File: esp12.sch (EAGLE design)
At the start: 26 parts, among them IC1 117\33

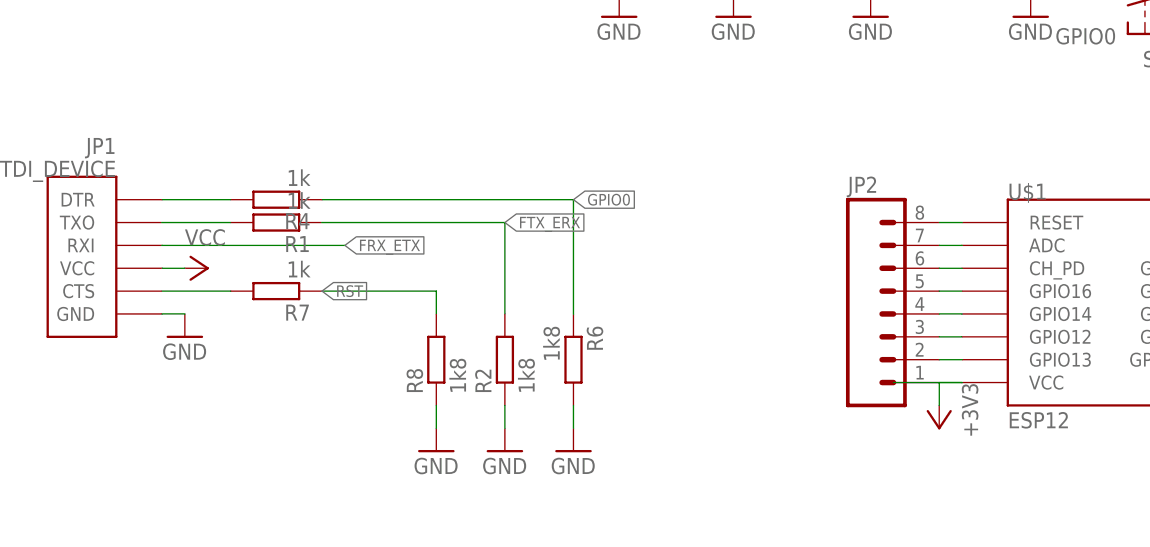
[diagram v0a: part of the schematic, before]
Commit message: gitignore and ADC 5V to 1.8V conversion
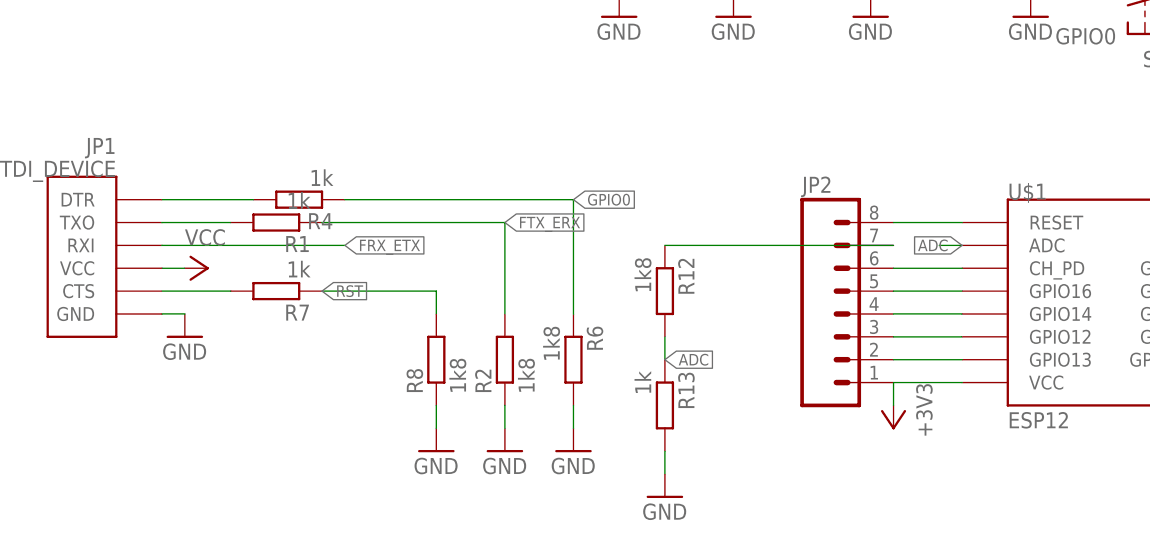
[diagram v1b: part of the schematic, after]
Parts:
- added R12: 1k8, resistor:R-EU_M1206
- added R13: 1k, resistor:R-EU_M1206
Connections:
- new net ADC: R12.2, R13.1, U$1.ADC
- net GND: now also R13.2
- net N$9: now also R12.1; no longer U$1.ADC
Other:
- moved on the sheet: JP2, R4
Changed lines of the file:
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@@
 <part name="GND11" library="supply1" deviceset="GND" device=""/>
 <part name="R11" library="resistor" deviceset="R-EU_" device="M1206" value="10k"/>
+<part name="R12" library="resistor" deviceset="R-EU_" device="M1206" value="1k8"/>
+<part name="R13" library="resistor" deviceset="R-EU_" device="M1206" value="1k"/>
+<part name="GND14" library="supply1" deviceset="GND" device=""/>
 </parts>
 <sheets>
@@
 <instance part="GND7" gate="1" x="63.5" y="71.12"/>
 <instance part="U$1" gate="G$1" x="73.66" y="40.64"/>
-<instance part="+3V2" gate="G$1" x="53.34" y="25.4" rot="R180"/>
-<instance part="JP2" gate="G$1" x="48.26" y="38.1"/>
+<instance part="+3V2" gate="G$1" x="48.26" y="25.4" rot="R180"/>
+<instance part="JP2" gate="G$1" x="43.18" y="38.1"/>
 <instance part="JP3" gate="G$1" x="96.52" y="38.1" rot="MR0"/>
 <instance part="S2" gate="1" x="76.2" y="88.9" rot="R90"/>
@@
 <instance part="GND10" gate="1" x="63.5" y="104.14"/>
 <instance part="+3V6" gate="G$1" x="96.52" y="116.84"/>
-<instance part="R4" gate="G$1" x="-20.32" y="50.8" rot="R180"/>
+<instance part="R4" gate="G$1" x="-17.78" y="50.8" rot="R180"/>
 <instance part="R6" gate="G$1" x="12.7" y="33.02" rot="R270"/>
 <instance part="GND12" gate="1" x="12.7" y="22.86"/>
@@
 <instance part="GND11" gate="1" x="-12.7" y="104.14" rot="R180"/>
 <instance part="R11" gate="G$1" x="-12.7" y="91.44" rot="R270"/>
+<instance part="R12" gate="G$1" x="22.86" y="40.64" rot="R270"/>
+<instance part="R13" gate="G$1" x="22.86" y="27.94" rot="R270"/>
+<instance part="GND14" gate="1" x="22.86" y="17.78"/>
 </instances>
 <busses>
@@
 <wire x1="-12.7" y1="101.6" x2="-12.7" y2="96.52" width="0.1524" layer="91"/>
 </segment>
+<segment>
+<pinref part="R13" gate="G$1" pin="2"/>
+<pinref part="GND14" gate="1" pin="GND"/>
+<wire x1="22.86" y1="22.86" x2="22.86" y2="20.32" width="0.1524" layer="91"/>
+</segment>
 </net>
 <net name="+3V3" class="0">
@@
 <pinref part="JP2" gate="G$1" pin="1"/>
 <pinref part="JP2" gate="G$1" pin="1"/>
-<wire x1="53.34" y1="30.48" x2="53.34" y2="27.94" width="0.1524" layer="91"/>
-<wire x1="48.26" y1="30.48" x2="55.88" y2="30.48" width="0.1524" layer="91"/>
-<wire x1="55.88" y1="30.48" x2="53.34" y2="30.48" width="0.1524" layer="91"/>
+<wire x1="48.26" y1="30.48" x2="48.26" y2="27.94" width="0.1524" layer="91"/>
+<wire x1="55.88" y1="30.48" x2="48.26" y2="30.48" width="0.1524" layer="91"/>
 </segment>
 <segment>
@@
 <pinref part="U$1" gate="G$1" pin="GPIO13"/>
 <pinref part="JP2" gate="G$1" pin="2"/>
-<wire x1="53.34" y1="33.02" x2="55.88" y2="33.02" width="0.1524" layer="91"/>
+<wire x1="48.26" y1="33.02" x2="55.88" y2="33.02" width="0.1524" layer="91"/>
 </segment>
 </net>
@@
 <pinref part="U$1" gate="G$1" pin="GPIO12"/>
 <pinref part="JP2" gate="G$1" pin="3"/>
-<wire x1="53.34" y1="35.56" x2="55.88" y2="35.56" width="0.1524" layer="91"/>
+<wire x1="48.26" y1="35.56" x2="55.88" y2="35.56" width="0.1524" layer="91"/>
 </segment>
 </net>
@@
 <pinref part="U$1" gate="G$1" pin="GPIO14"/>
 <pinref part="JP2" gate="G$1" pin="4"/>
-<wire x1="53.34" y1="38.1" x2="55.88" y2="38.1" width="0.1524" layer="91"/>
+<wire x1="48.26" y1="38.1" x2="55.88" y2="38.1" width="0.1524" layer="91"/>
 </segment>
 </net>
@@
 <pinref part="U$1" gate="G$1" pin="GPIO16"/>
 <pinref part="JP2" gate="G$1" pin="5"/>
-<wire x1="53.34" y1="40.64" x2="55.88" y2="40.64" width="0.1524" layer="91"/>
-</segment>
-</net>
-<net name="N$9" class="0">
-<segment>
-<pinref part="U$1" gate="G$1" pin="ADC"/>
-<pinref part="JP2" gate="G$1" pin="7"/>
-<wire x1="53.34" y1="45.72" x2="55.88" y2="45.72" width="0.1524" layer="91"/>
+<wire x1="48.26" y1="40.64" x2="55.88" y2="40.64" width="0.1524" layer="91"/>
 </segment>
 </net>
@@
 <pinref part="R6" gate="G$1" pin="1"/>
 <wire x1="12.7" y1="38.1" x2="12.7" y2="50.8" width="0.1524" layer="91"/>
-<wire x1="12.7" y1="50.8" x2="-15.24" y2="50.8" width="0.1524" layer="91"/>
+<wire x1="12.7" y1="50.8" x2="-12.7" y2="50.8" width="0.1524" layer="91"/>
 <label x="12.7" y="50.8" size="1.27" layer="95" xref="yes"/>
 </segment>
@@
 <pinref part="U$1" gate="G$1" pin="RESET"/>
 <pinref part="JP2" gate="G$1" pin="8"/>
-<wire x1="53.34" y1="48.26" x2="55.88" y2="48.26" width="0.1524" layer="91"/>
+<wire x1="48.26" y1="48.26" x2="55.88" y2="48.26" width="0.1524" layer="91"/>
 </segment>
 <segment>
@@
 <pinref part="JP1" gate="G$1" pin="DTR"/>
 <pinref part="R4" gate="G$1" pin="2"/>
-<wire x1="-25.4" y1="50.8" x2="-33.02" y2="50.8" width="0.1524" layer="91"/>
+<wire x1="-22.86" y1="50.8" x2="-33.02" y2="50.8" width="0.1524" layer="91"/>
 </segment>
 </net>
@@
 <pinref part="U$1" gate="G$1" pin="CH_PD"/>
 <pinref part="JP2" gate="G$1" pin="6"/>
-<wire x1="53.34" y1="43.18" x2="55.88" y2="43.18" width="0.1524" layer="91"/>
+<wire x1="48.26" y1="43.18" x2="55.88" y2="43.18" width="0.1524" layer="91"/>
 </segment>
 <segment>
@@
 </segment>
 </net>
+<net name="N$9" class="0">
+<segment>
+<pinref part="JP2" gate="G$1" pin="7"/>
+<pinref part="R12" gate="G$1" pin="1"/>
+<wire x1="22.86" y1="45.72" x2="48.26" y2="45.72" width="0.1524" layer="91"/>
+</segment>
+</net>
+<net name="ADC" class="0">
+<segment>
+<pinref part="U$1" gate="G$1" pin="ADC"/>
+<wire x1="55.88" y1="45.72" x2="53.34" y2="45.72" width="0.1524" layer="91"/>
+<label x="55.88" y="45.72" size="1.27" layer="95" rot="R180" xref="yes"/>
+</segment>
+<segment>
+<pinref part="R12" gate="G$1" pin="2"/>
+<pinref part="R13" gate="G$1" pin="1"/>
+<wire x1="22.86" y1="35.56" x2="22.86" y2="33.02" width="0.1524" layer="91"/>
+<label x="22.86" y="33.02" size="1.27" layer="95" xref="yes"/>
+</segment>
+</net>

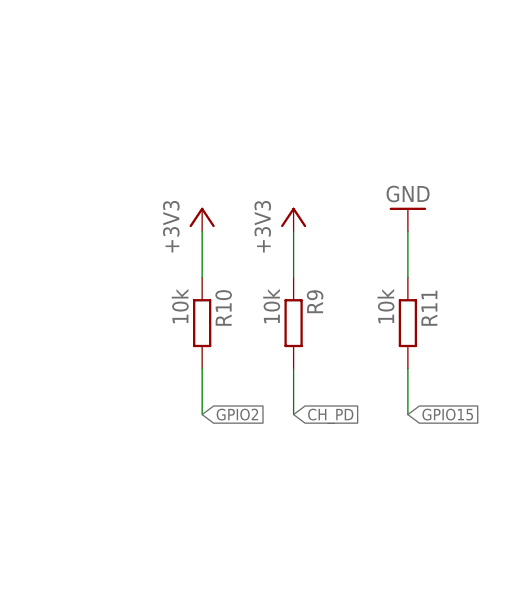
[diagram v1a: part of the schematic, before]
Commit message: LED for GPIO0 added
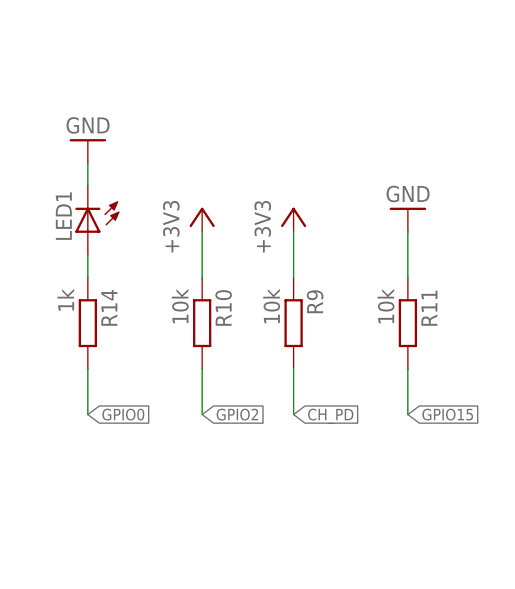
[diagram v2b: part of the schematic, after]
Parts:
- added LED1: (no value), led:LEDSMT1206
- added R14: 1k, resistor:R-EU_M1206
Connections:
- new net N$8: LED1.A, R14.1
- net GND: now also LED1.C
- net GPIO0: now also R14.2
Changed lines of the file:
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@@
 <part name="R13" library="resistor" deviceset="R-EU_" device="M1206" value="1k"/>
 <part name="GND14" library="supply1" deviceset="GND" device=""/>
+<part name="LED1" library="led" deviceset="LED" device="SMT1206"/>
+<part name="R14" library="resistor" deviceset="R-EU_" device="M1206" value="1k"/>
+<part name="GND15" library="supply1" deviceset="GND" device=""/>
 </parts>
 <sheets>
@@
 <instance part="R13" gate="G$1" x="22.86" y="27.94" rot="R270"/>
 <instance part="GND14" gate="1" x="22.86" y="17.78"/>
+<instance part="LED1" gate="G$1" x="-48.26" y="101.6" rot="R180"/>
+<instance part="R14" gate="G$1" x="-48.26" y="91.44" rot="R270"/>
+<instance part="GND15" gate="1" x="-48.26" y="111.76" rot="R180"/>
 </instances>
 <busses>
@@
 <wire x1="22.86" y1="22.86" x2="22.86" y2="20.32" width="0.1524" layer="91"/>
 </segment>
+<segment>
+<pinref part="LED1" gate="G$1" pin="C"/>
+<pinref part="GND15" gate="1" pin="GND"/>
+<wire x1="-48.26" y1="109.22" x2="-48.26" y2="106.68" width="0.1524" layer="91"/>
+</segment>
 </net>
 <net name="+3V3" class="0">
@@
 <label x="12.7" y="50.8" size="1.27" layer="95" xref="yes"/>
 </segment>
+<segment>
+<pinref part="R14" gate="G$1" pin="2"/>
+<wire x1="-48.26" y1="86.36" x2="-48.26" y2="81.28" width="0.1524" layer="91"/>
+<label x="-48.26" y="81.28" size="1.27" layer="95" xref="yes"/>
+</segment>
 </net>
 <net name="GPIO2" class="0">
@@
 </segment>
 </net>
+<net name="N$8" class="0">
+<segment>
+<pinref part="LED1" gate="G$1" pin="A"/>
+<pinref part="R14" gate="G$1" pin="1"/>
+<wire x1="-48.26" y1="96.52" x2="-48.26" y2="99.06" width="0.1524" layer="91"/>
+</segment>
+</net>
